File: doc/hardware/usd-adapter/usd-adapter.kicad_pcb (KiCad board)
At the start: 2 copper layers, 16.9 x 34.9 mm, 2 parts, among them J1 usd-plug, P1 CONN_02X04

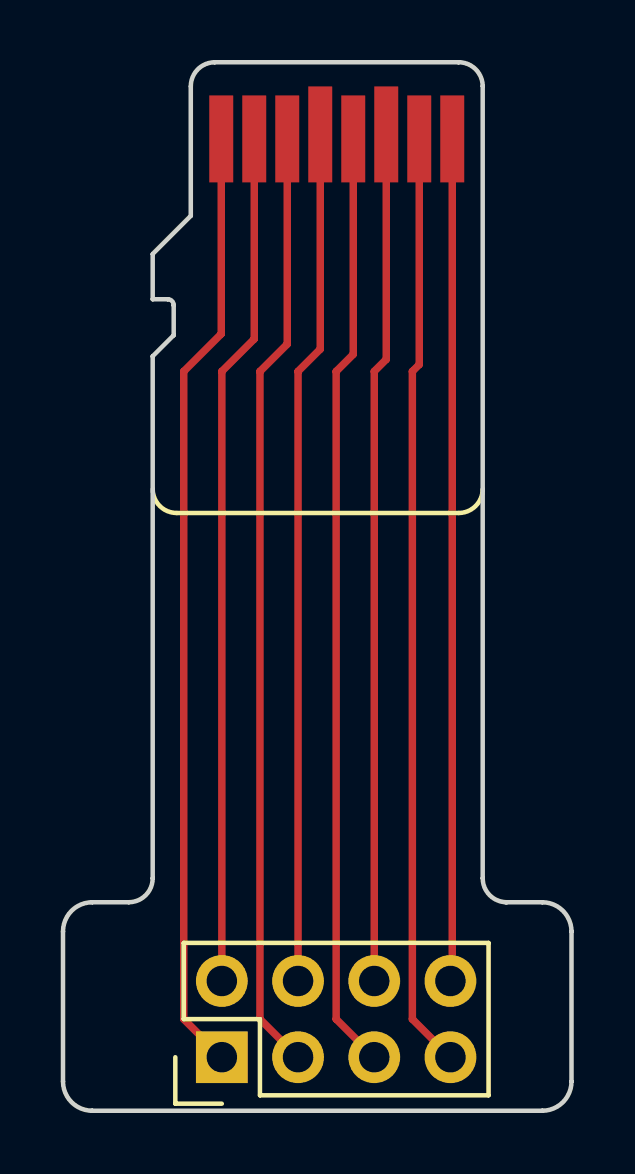
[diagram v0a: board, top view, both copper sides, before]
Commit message: Change via's shape to oval and check manufacturer requirements
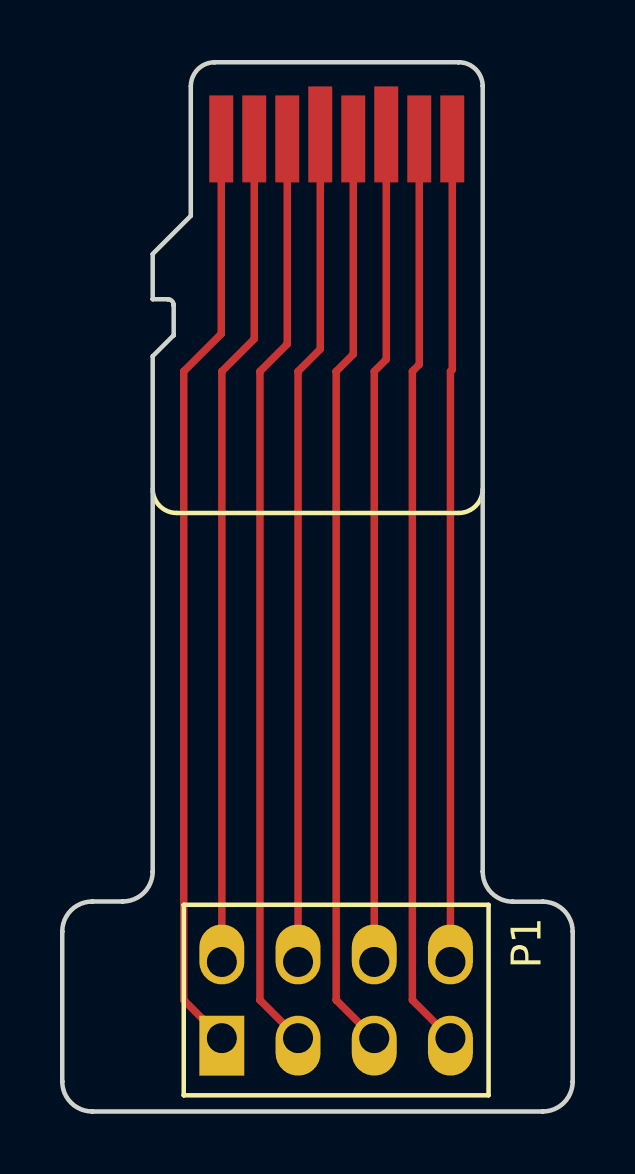
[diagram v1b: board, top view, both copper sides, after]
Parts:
- P1: footprint Pin_Headers:Pin_Header_Straight_2x04 -> connectors:PSB_IDC_4x2
- moved P1 4.26 mm to (151.1, 121.3), turned to 0 degrees
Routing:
- net /N8: track 28.1 -> 27.5 mm
- net /N6: track 28.4 -> 27.8 mm
- net /N4: track 28.5 -> 27.9 mm
- net /N2: track 28.5 -> 27.9 mm
- net /N1: track 31.7 -> 31.0 mm
- net /N7: track 31.2 -> 30.6 mm
- net /N5: track 31.4 -> 30.7 mm
- net /N3: track 31.5 -> 30.9 mm
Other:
- board size 16.9 x 34.9 mm -> 17 x 35 mm
- net class Default: clearance 0.2 -> 0.1524
- rule trace_clearance: 0.2 -> 0.1524
- rule trace_min: 0.2 -> 0.1524
